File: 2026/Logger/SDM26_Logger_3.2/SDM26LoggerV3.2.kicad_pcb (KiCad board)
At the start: 4 copper layers, 75 x 87 mm, 128 parts, among them IC1 ESP32-S3-WROOM-1-N8R8, IC2 CP2102N-A02-GQFN28, IC3 MIC37100-3.3WS, IC4 TPS563211DRLR, IC5 MIC37100-3.3WS, IC6 NEO-F9P-15B, J1 UART_USB, J2 ESP_USB, J3 GNSS_Debug, J4 Molex_1040310811, J5 1-776087-4, J6 1-776087-4, K1 IMB03IGR, Q1 MMBT2222LT1G, Q2 MMBT2222LT1G, U1 INA260, U10 EMIF06-MSD02N16, U2 USBLC6-2SC6, U3 TPS2116DRL, U4 USBLC6-2SC6, U5 USBLC6-2SC6, U6 TPS2116, U7 SN65HVD230, U8 ADR425BRZ, U9 ADC128S102, Y1 ECX-.327-CDX-2096

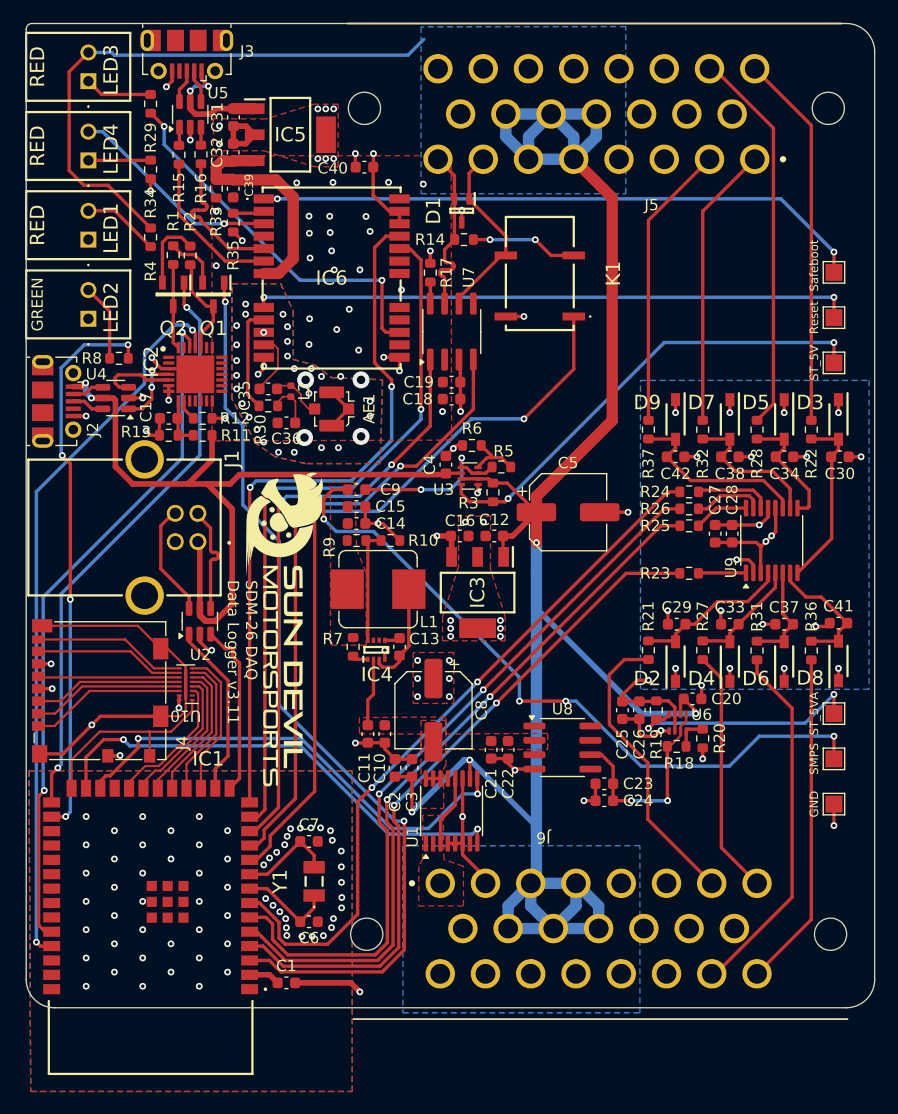
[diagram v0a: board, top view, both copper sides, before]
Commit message: update voltage divider to more common values and changed CAN termination to MOSFET
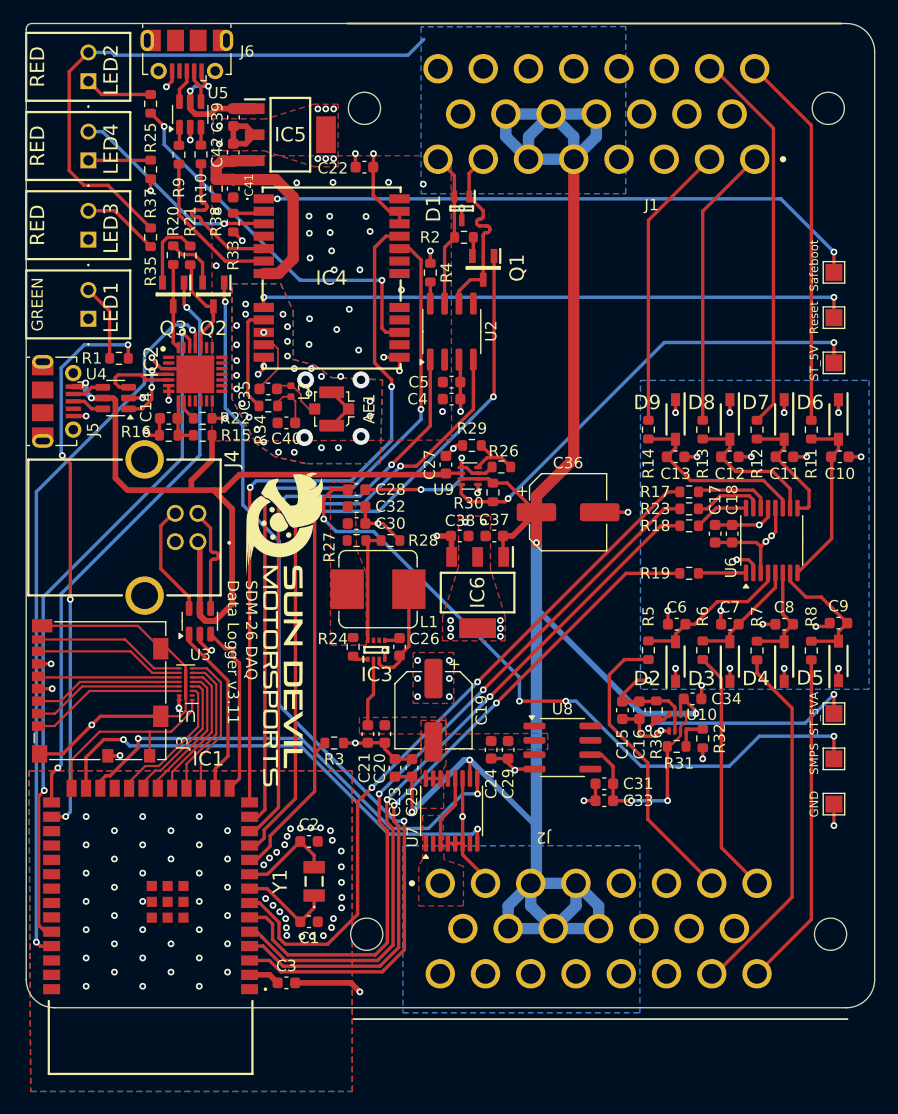
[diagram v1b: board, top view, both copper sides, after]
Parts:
- removed K1: IMB03IGR, SDM_MiscFootprint:IMB03IGR
- added Q1: MMBT2222LT1G, SDM_MiscFootprint:SOT96P237X111-3N, F.Cu at (129.9, 91.6)
- added R3: 10k, Resistor_SMD:R_0603_1608Metric, F.Cu at (116.7, 133.6)
- moved D1 0.20 mm to (128.0, 86.3)
- moved R2 0.20 mm to (128.2, 88.9)
- renumbered C6 to C1, C30 to C10, C34 to C11, C38 to C12, C42 to C13, C17 to C14, C25 to C15, C26 to C16, C27 to C17, C28 to C18, C8 to C19, C7 to C2, C10 to C20, C11 to C21, C40 to C22, C2 to C23, C21 to C24, C3 to C25, C13 to C26, C4 to C27, C9 to C28, C22 to C29, C1 to C3, C14 to C30, C23 to C31, C15 to C32, C24 to C33, C20 to C34, C5 to C36, C12 to C37, C16 to C38, C31 to C39, C18 to C4, C36 to C40, C39 to C41, C32 to C42, C19 to C5, C29 to C6, C33 to C7, C37 to C8, C41 to C9, D4 to D3, D6 to D4, D8 to D5, D3 to D6, D5 to D7, D7 to D8, IC4 to IC3, IC6 to IC4, IC3 to IC6, J5 to J1, J6 to J2, J4 to J3, J1 to J4, J2 to J5, J3 to J6, LED2 to LED1, LED3 to LED2, LED1 to LED3, Q1 to Q2, Q2 to Q3, R8 to R1, R16 to R10, R22 to R11, R28 to R12, R32 to R13, R37 to R14, R11 to R15, R13 to R16, R24 to R17, R25 to R18, R23 to R19, R14 to R2, R1 to R20, R2 to R21, R12 to R22, R26 to R23, R7 to R24, R29 to R25, R5 to R26, R9 to R27, R10 to R28, R6 to R29, R3 to R30, R18 to R31, R20 to R32, R35 to R33, R30 to R34, R4 to R35, R19 to R36, R34 to R37, R33 to R38, R17 to R4, R21 to R5, R27 to R6, R31 to R7, R36 to R8, R15 to R9, TP3 to TP1, TP1 to TP3, TP5 to TP4, TP6 to TP5, TP4 to TP6, U10 to U1, U6 to U10, U7 to U2, U2 to U3, U9 to U6, U1 to U7, U3 to U9
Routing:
- net Net-(Q1-S): track 9.45 -> 1.68 mm, vias 2 -> 0
- net +5V: track 240.2 -> 237.4 mm
- net /CAN-: track 15.6 -> 17.0 mm
- net /CAN+: track 15.0 -> 13.7 mm
- net /CAN_TERM: track 66.0 -> 67.2 mm
- net VBUS: track 70.1 -> 70.8 mm
- net GND: track 133.4 -> 132.9 mm, vias 182 -> 181

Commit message: Adding Optocoupler for CAN termination
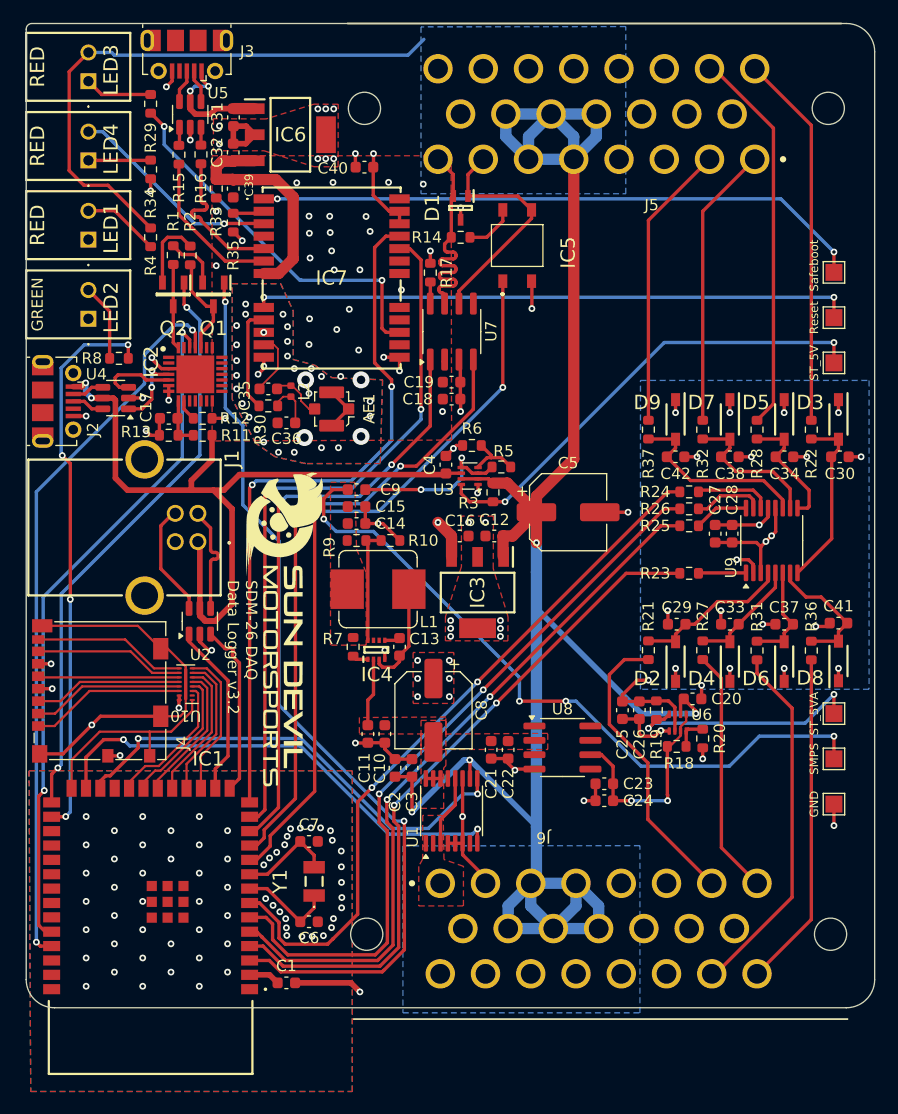
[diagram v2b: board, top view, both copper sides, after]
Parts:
- removed the Q1 at (129.9, 91.6)
- removed the R3 at (116.7, 133.6)
- added IC5: TLP175A_TPL,E, SDM_MiscFootprint:TLP266J, F.Cu at (132.9, 90.2)
- R10: renamed from R28; value 10k -> 11k
- R9: renamed from R27; value 74.1k -> 82k
- moved R14 0.30 mm to (127.9, 88.9)
- moved D1 0.11 mm to (127.9, 86.3)
- renumbered C3 to C1, C20 to C10, C21 to C11, C37 to C12, C26 to C13, C30 to C14, C32 to C15, C38 to C16, C14 to C17, C4 to C18, C5 to C19, C23 to C2, C34 to C20, C24 to C21, C29 to C22, C31 to C23, C33 to C24, C15 to C25, C16 to C26, C17 to C27, C18 to C28, C6 to C29, C25 to C3, C10 to C30, C39 to C31, C42 to C32, C7 to C33, C11 to C34, C40 to C36, C8 to C37, C12 to C38, C41 to C39, C27 to C4, C22 to C40, C9 to C41, C13 to C42, C36 to C5, C1 to C6, C2 to C7, C19 to C8, C28 to C9, D6 to D3, D3 to D4, D7 to D5, D4 to D6, D8 to D7, D5 to D8, IC6 to IC3, IC3 to IC4, IC5 to IC6, IC4 to IC7, J4 to J1, J5 to J2, J6 to J3, J3 to J4, J1 to J5, J2 to J6, LED3 to LED1, LED1 to LED2, LED2 to LED3, Q2 to Q1, Q3 to Q2, R20 to R1, R15 to R11, R22 to R12, R16 to R13, R2 to R14, R9 to R15, R10 to R16, R4 to R17, R31 to R18, R36 to R19, R21 to R2, R32 to R20, R5 to R21, R11 to R22, R19 to R23, R17 to R24, R18 to R25, R23 to R26, R6 to R27, R12 to R28, R25 to R29, R30 to R3, R34 to R30, R7 to R31, R13 to R32, R38 to R33, R37 to R34, R33 to R35, R8 to R36, R14 to R37, R35 to R4, R26 to R5, R29 to R6, R24 to R7, R1 to R8, TP3 to TP1, TP1 to TP3, TP6 to TP4, TP4 to TP5, TP5 to TP6, U7 to U1, U1 to U10, U3 to U2, U9 to U3, U10 to U6, U2 to U7, U6 to U9
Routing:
- net /CAN+: track 13.7 -> 20.1 mm
- net /CAN-: track 17.0 -> 20.9 mm
- net /CAN_TERM: track 67.2 -> 63.8 mm
- net Net-(IC5-Pad6): track 1.68 -> 4.49 mm
- net GND: track 132.9 -> 134.2 mm, vias 181 -> 182
- net /RF_IN: track 4.63 -> 4.12 mm
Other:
- board text added: "SDM-26 DAQ Data Logger v3.2"
- board text removed: "SDM-26 DAQ Data Logger v3.11"
